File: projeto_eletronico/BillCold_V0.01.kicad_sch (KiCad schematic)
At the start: 16 parts, among them J1 USB_B, U1 ESP32-S3, U2 AMS1117

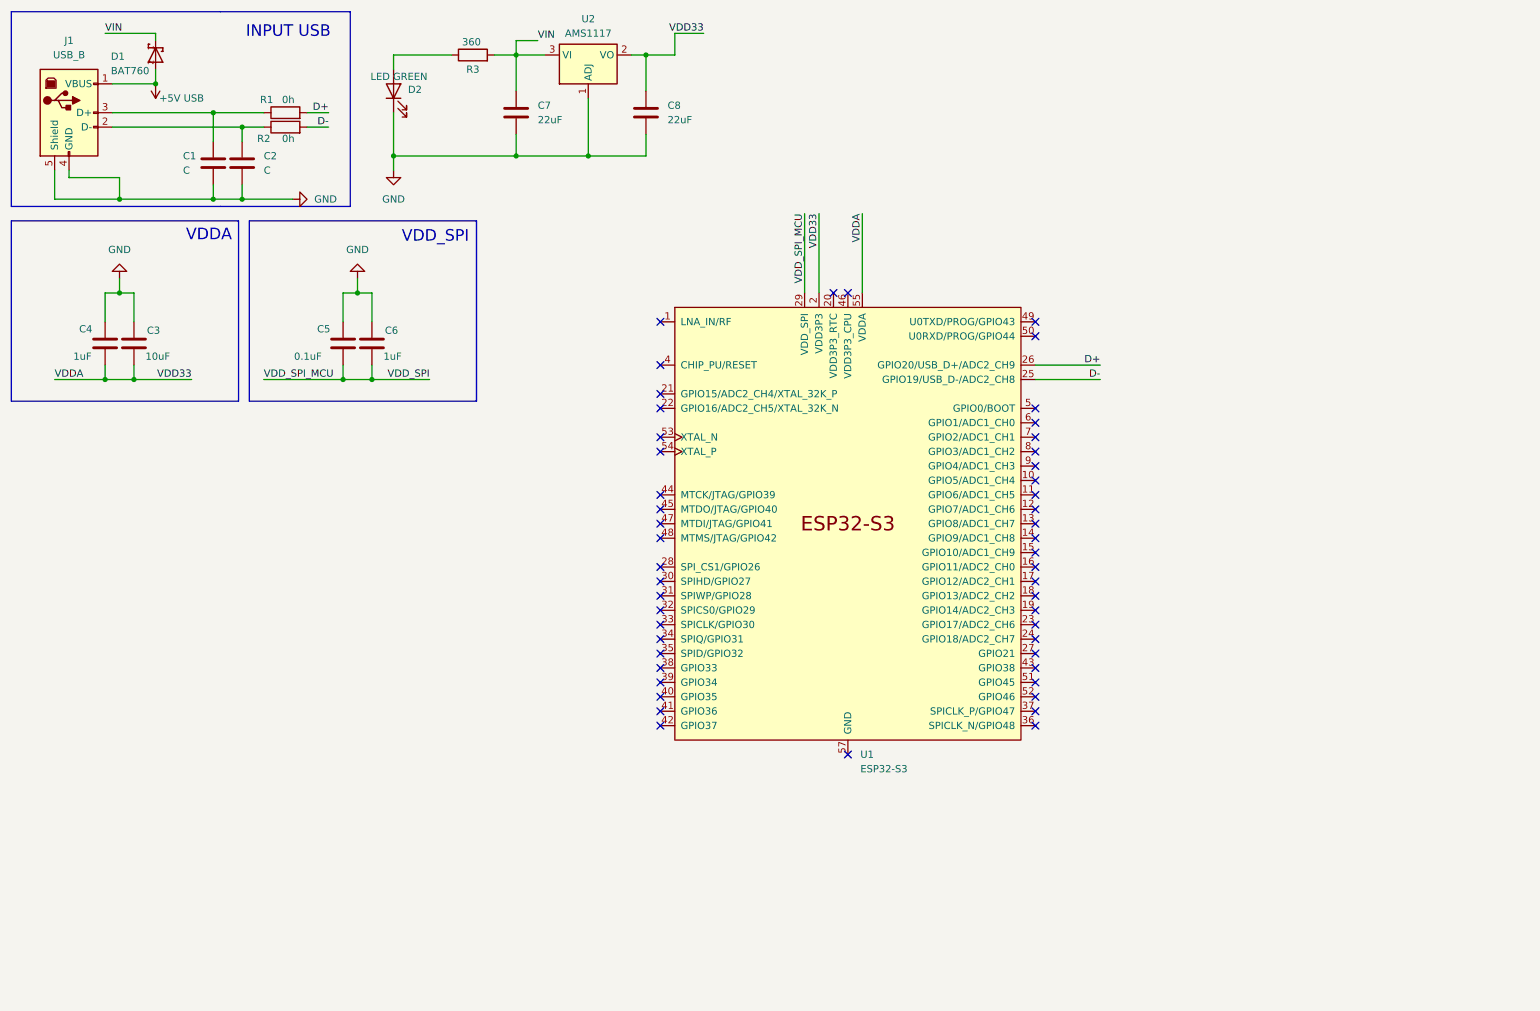
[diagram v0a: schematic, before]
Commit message: Finalizando o projeto do harware do mcu
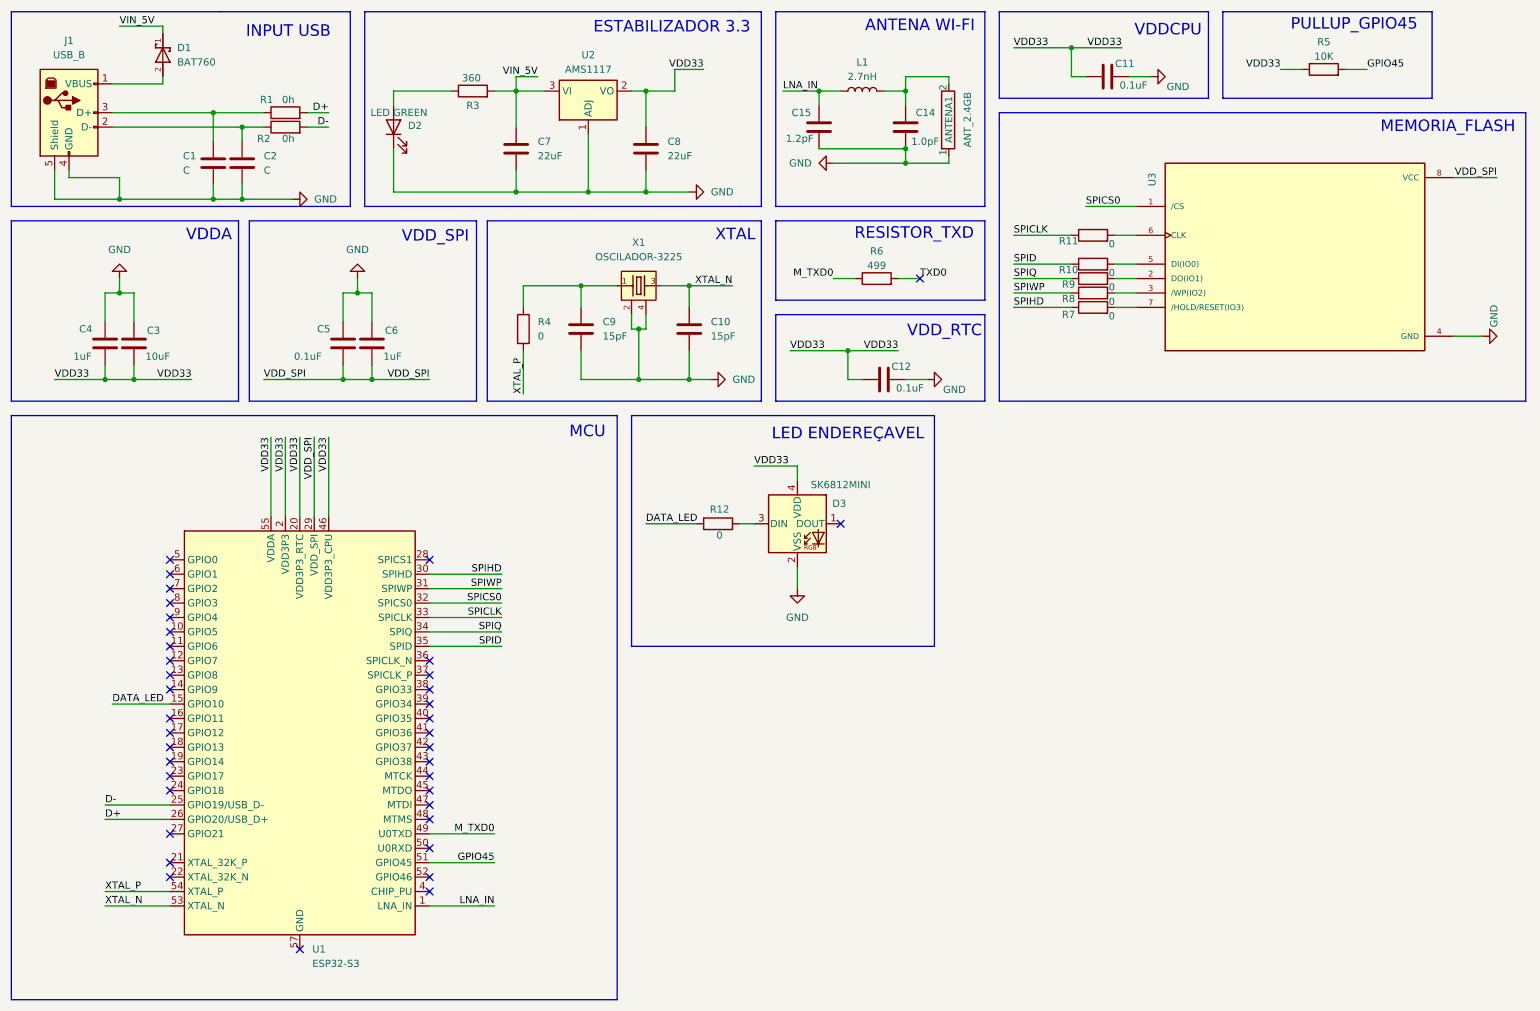
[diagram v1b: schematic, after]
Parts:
- removed U1: ESP32-S3, Package_DFN_QFN:QFN-56-1EP_7x7mm_P0.4mm_EP5.6x5.6mm, symbol ESP_32_OFICIAL:ESP32-S3
- added ANTENA1: ANT_2.4GB, ANTENA_2.4GZ:Antena_2.4GB, symbol ANTENA_2.4GZ:ANT_2.4GB
- added C10, C9: 15pF, Capacitor_SMD:C_1206_3216Metric, symbol Device:C
- added C11, C12: 0.1uF, Capacitor_SMD:C_1206_3216Metric, symbol Device:C
- added C14: 1.0pF, Inductor_SMD:L_0805_2012Metric, symbol Device:C
- added C15: 1.2pF, Capacitor_SMD:C_1206_3216Metric, symbol Device:C
- added D3: SK6812MINI, LED_SMD:LED_SK6812MINI_PLCC4_3.5x3.5mm_P1.75mm, symbol LED:SK6812MINI
- added L1: 2.7nH, Inductor_SMD:L_0805_2012Metric, symbol Device:L
- added R10, R11, R12, R4, R7, R8, R9: 0, Resistor_SMD:R_1206_3216Metric, symbol Device:R
- added R5: 10K, Resistor_SMD:R_1206_3216Metric, symbol Device:R
- added R6: 499, Resistor_SMD:R_1206_3216Metric, symbol Device:R
- added U1: ESP32-S3, Package_DFN_QFN:QFN-56-1EP_7x7mm_P0.4mm_EP4x4mm, symbol MCU_Espressif:ESP32-S3
- added U3: W25Q128JVSIQ, MEMORIA_FLESH:SOIC127P790X216-8N, symbol MEMORIA_FLESH:W25Q128JVSIQ
- added X1: OSCILADOR-3225, OSCILADOR_3225:TSX-3225, symbol OSCILADOR_3225:TSX-3225
- C7, C8: footprint (none) -> Capacitor_SMD:C_1206_3216Metric
- D2: footprint (none) -> LED_SMD:LED_1206_3216Metric
- R3: footprint (none) -> Resistor_SMD:R_1206_3216Metric
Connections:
- net D+: now also U1.26 (GPIO20/USB_D+)
- net D-: now also U1.25 (GPIO19/USB_D-)
- net GND: now also ANTENA1.1, C10.2, C11.2, C12.2, C14.2, C15.2, C9.2, D3.2 (VSS), U3.4 (GND), X1.2, X1.4
- net VDD_SPI: now also U1.29 (VDD_SPI), U3.8 (VCC)
- net +5V USB: no longer names the net of D1.2, J1.1 (VBUS)
- net VDD3P3 renamed VDD33
- net VDD33: now also C11.1, C12.1, D3.4 (VDD), R5.1, U1.2 (VDD3P3), U1.20 (VDD3P3_RTC), U1.3 (VDD3P3), U1.46 (VDD3P3_CPU), U1.55 (VDDA), U1.56 (VDDA)
- net VIN renamed VIN_5V
- new net: R10.2, U3.5 (DI(IO0))
- new net: C9.1, R4.1, X1.1
- new net: ANTENA1.2, C14.1, L1.2
- new net: R8.2, U3.3 (/WP(IO2))
- new net: D3.3 (DIN), R12.2
- new net: R7.2, U3.7 (/HOLD/RESET(IO3))
- new net: R11.2, U3.6 (CLK)
- new net: R9.2, U3.2 (DO(IO1))
- new net DATA_LED: R12.1, U1.15 (GPIO10)
- new net GPIO45: R5.2, U1.51 (GPIO45)
- new net LNA_IN: C15.1, L1.1, U1.1 (LNA_IN)
- new net M_TXD0: R6.1, U1.49 (U0TXD)
- new net SPICLK: R11.1, U1.33 (SPICLK)
- new net SPICS0: U1.32 (SPICS0), U3.1 (/CS)
- new net SPID: R10.1, U1.35 (SPID)
- new net SPIHD: R7.1, U1.30 (SPIHD)
- new net SPIQ: R9.1, U1.34 (SPIQ)
- new net SPIWP: R8.1, U1.31 (SPIWP)
- new net TXD0: R6.2
- new net XTAL_N: C10.1, U1.53 (XTAL_N), X1.3
- new net XTAL_P: R4.2, U1.54 (XTAL_P)
- no-connect marks 50 -> 38
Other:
- note added: "ANTENA WI-FI"
- note added: "ESTABILIZADOR 3.3"
- note added: "LED ENDEREÇAVEL"
- note added: "MCU"
- note added: "MEMORIA_FLASH"
- note added: "PULLUP_GPIO45"
- note added: "RESISTOR_TXD"
- note added: "VDDCPU"
- note added: "VDD_RTC"
- note added: "XTAL"
- moved on the sheet: C7, C8, D2, R3, U2
